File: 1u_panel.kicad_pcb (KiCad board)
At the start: 2 copper layers, 83 x 100 mm, 74 parts, among them J1 PPPC021LFBN-RC, J2 2-1734592-0, J3 PPTC041LFBN-RC, Q1 DMP3050LVT-7, Q2 DMP2240UDM-7, U1 TCAN330GDCNT, U12 LTC4412, U4 INA226AIDGSR, U5 LTC3525D-3.3, U7 STM32F091CCT7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

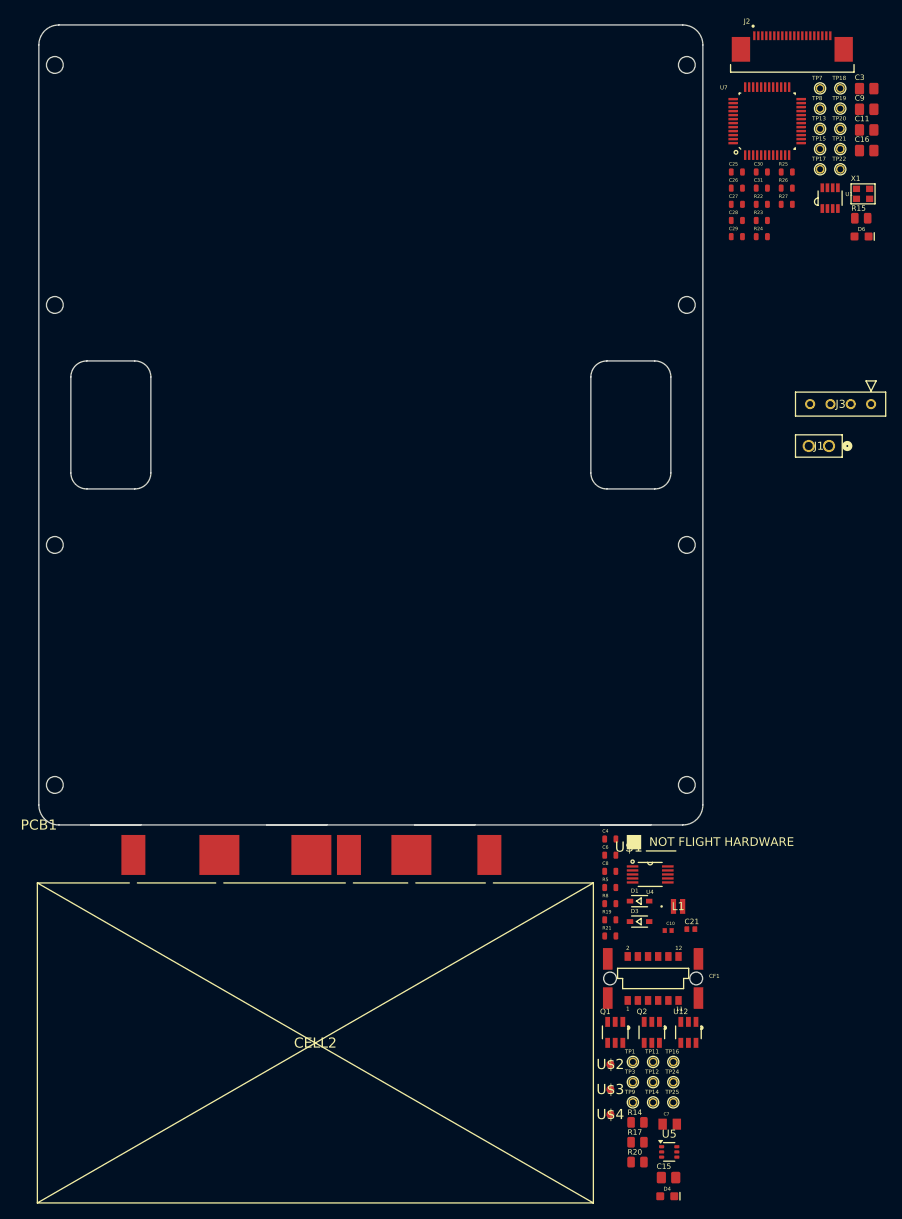
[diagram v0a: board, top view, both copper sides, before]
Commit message: Layout draft
Note that there's currently no footprint for the panels; need to make one based on the panels we have in storage
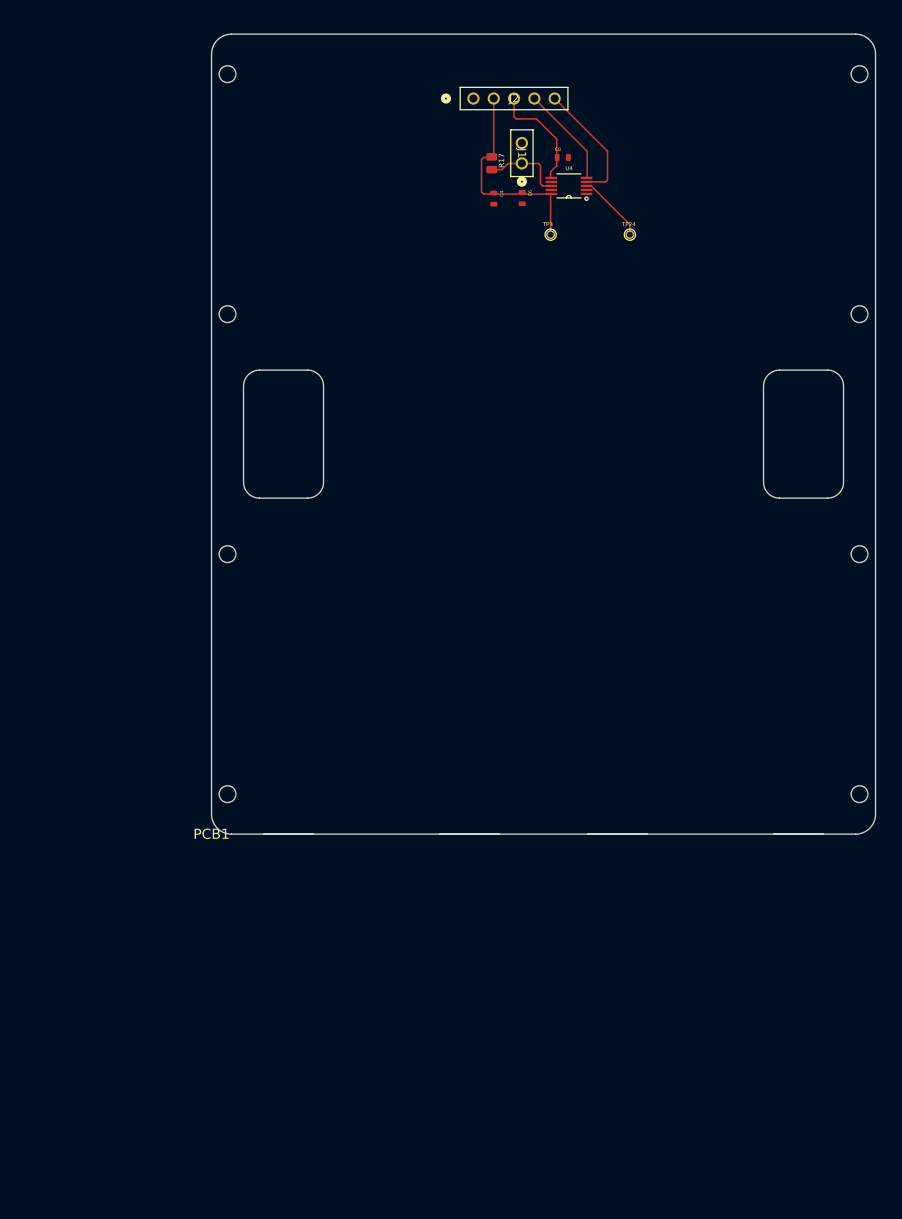
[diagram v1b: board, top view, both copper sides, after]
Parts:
- removed C10: GRM155R70J105KA12D, GRM155R70J105KA12D:CAPC1005X55N
- removed C11, C15, C16, C3, C9: 22u, 1u_panel:.0805-B-NOSILK
- removed C21: 100n, 1u_panel:.0402-B-NOSILK
- removed C25, C26, C29, C30, C31: 100n, 1u_panel:.0603-C-NOSILK
- removed C27, C28: 20p, 1u_panel:.0603-C-NOSILK
- removed C7: GRM219R60J106KE19D, GRM219R60J106KE19D:CAPC2012X95N
- removed CELL2: SPECTROLAB-XTE-SF, 1u_panel:SPECTROLAB-XTE-SF
- removed CF1: M55-6021242R, 1u_panel:HARWIN-M55-60X1242R
- removed D1, D3: 1N4151WS, 1u_panel:SOD323-R
- removed D4: GREEN, 1u_panel:LED-0603
- removed D6: AMBER, 1u_panel:LED-0603
- removed J3: PPTC041LFBN-RC, conn-4pin:CONN_PPTC041LFBN-RC_SUL
- removed L1: XFL2010-682MEC, IND_XFL2010_COC:IND_XFL2010_COC
- removed Q1: DMP3050LVT-7, 1u_panel:SOT23-6
- removed Q2: DMP2240UDM-7, 1u_panel:SOT23-6
- removed R14, R15, R20: 0, 1u_panel:.0805-C-NOSILK
- removed R19, R8: 100k, 1u_panel:.0603-C-NOSILK
- removed R21, R23: 2.7k, 1u_panel:.0603-C-NOSILK
- removed R22: 10k, 1u_panel:.0603-C-NOSILK
- removed R24, R25, R26, R27: 1k/NP, 1u_panel:.0603-C-NOSILK
- removed R5: 200k, 1u_panel:.0603-C-NOSILK
- removed TP1, TP11, TP12, TP13, TP14, TP15, TP16, TP17, TP18, TP19, TP20, TP21, TP22, TP25, TP7, TP8, TP9: TEST-POINT-LARGE-SQUARE, 1u_panel:1X01
- removed U$1: FLIGHMARKERNEW, 1u_panel:FLIGHTMARKER_NEW_BOARDS
- removed U$2, U$3, U$4: FIDUCIAL, 1u_panel:FIDUCIAL_1MM
- removed U1: TCAN330GDCNT, 1u_panel:SOT23-8_TI-DCN
- removed U12: LTC4412, 1u_panel:SOT23-6
- removed U5: LTC3525D-3.3, Package_TO_SOT_SMD:SOT-363_SC-70-6
- removed U7: STM32F091CCT7, 1u_panel:STM32F091C
- removed X1: ECS-160-10-36Q-ES-TR, 1u_panel:CRYSTAL_2.5X2
- J2: value 2-1734592-0 -> PPTC051LFBN-RC; footprint J-TE-2-1734592-0:J-TE-2-1734592-0 -> conn-5pin:CONN5_1LFBN-RC_SUL
- moved R17 123.7 mm to (88.4, 40.3), turned to -90 degrees
- moved TP3 106.4 mm to (95.8, 49.3)
- moved TP24 106.1 mm to (105.7, 49.3)
- moved C8 89.4 mm to (97.3, 39.6)
- moved U4 86.7 mm to (98.0, 43.2), turned to 180 degrees
- moved C6 82.9 mm to (92.2, 44.7), turned to -90 degrees
- moved C4 81.4 mm to (88.6, 44.8), turned to -90 degrees
- moved J1 52.2 mm to (92.2, 40.4), turned to -90 degrees
- moved J2 40.6 mm to (86.1, 32.3)
- moved PCB1 21.6 mm to (53.4, 124.2)
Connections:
- C4 pad 1: V_SOLAR -> VSOLAR
- C6 pad 1: V_SOLAR -> VSOLAR
- J2 pad 1: Net-(J2-VBUSP-Pad1) -> GND
- J2 pad 2: Net-(J2-VBUSP-Pad1) -> VSOLAR
- J2 pad 3: GND -> 3.3V
- J2 pad 4: unconnected-(J2-DEVICE-D+-Pad4) -> SCL
- J2 pad 5: unconnected-(J2-DEVICE-D--Pad5) -> SDA
- R17 pad 1: V_SOLAR -> VSOLAR
- TP3 pad 1: V_SOLAR -> VSOLAR
- U4 pad 10: V_SOLAR -> VSOLAR

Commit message: MOST RECENT PCB LAYOUT
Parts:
- removed PCB1: ORESAT-SOLAR-BOARD-V4-SPECTROLABS, 1u_panel:ORESAT-SOLAR-BOARD-V4
- moved TP24 70.1 mm to (37.1, 63.8)
- moved U4 60.9 mm to (39.3, 59.2)
- moved C8 56.8 mm to (42.2, 53.7)
- moved TP3 56.5 mm to (41.1, 63.8)
- moved J1 47.5 mm to (46.9, 54.9), turned to 90 degrees
- moved J2 47.5 mm to (40.4, 45.0)
- moved C4 46.0 mm to (45.9, 61.8)
- moved C6 45.1 mm to (50.5, 61.9)
- moved R17 40.1 mm to (50.8, 54.2)
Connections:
- J2 pad 2: VSOLAR -> SDA
- J2 pad 3: 3.3V -> SCL
- J2 pad 4: SCL -> 3.3V
- J2 pad 5: SDA -> VSOLAR
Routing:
- net VSOLAR: track 0.00 -> 30.8 mm
- net SDA: track 0.00 -> 21.7 mm
- net SCL: track 0.00 -> 21.0 mm
- net 3.3V: track 0.00 -> 19.2 mm
- net Net-(U4-VBUS): track 0.00 -> 10.8 mm
- net Net-(U4-ALERT): track 0.00 -> 7.09 mm
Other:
- board outline removed
- board text added: "INA footprint is flipped"
